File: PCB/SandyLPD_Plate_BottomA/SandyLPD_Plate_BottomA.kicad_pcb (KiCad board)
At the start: 2 copper layers, 127.4 x 83 mm, 163 parts, among them J1 Conn_02x02_Odd_Even, J2 Conn_01x03, J4 Conn_01x10_Pin, J5 USB_C_Receptacle_USB2.0, J6 USB_C_Receptacle_USB2.0, SW1 BOOT_ALT, SW2 RESET_ALT, SW3 SW_DIP_x04, U1 NCP1117-3.3_SOT223, U3 RP2040, U4 W25Q128JVPIQ, Y1 12MHz

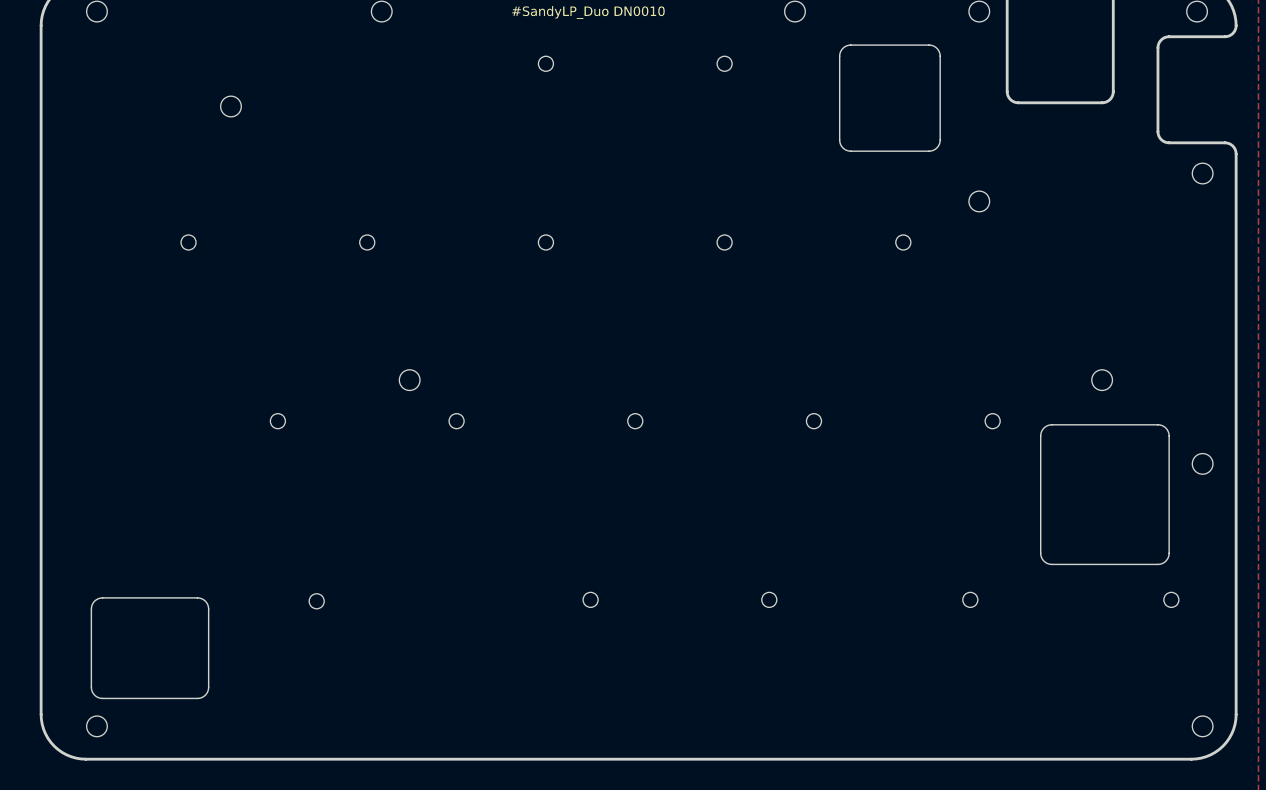
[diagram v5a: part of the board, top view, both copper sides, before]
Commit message: ボトムプレートの穴を大きく
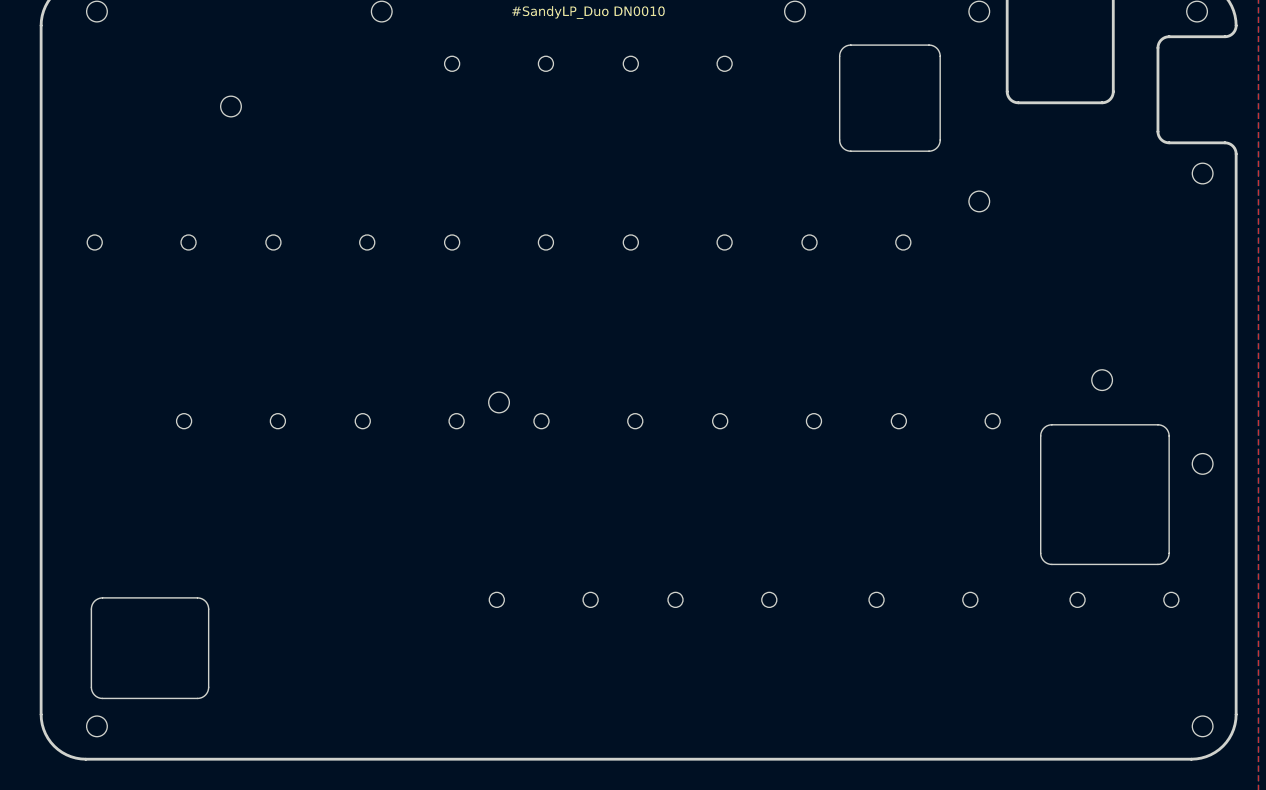
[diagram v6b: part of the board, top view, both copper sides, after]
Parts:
- removed H1, H10, H11, H12, H14, H15, H16, H17, H2, H3, H4, H5, H6, H7, H8, H9: MountingHole, locallib:Kailh_socket_ChocV2_cutout_type2
- removed H13: MountingHole, locallib:Kailh_socket_ChocV2_and_RotaryEncoder_cutout_type2
- moved H_btm_1 9.82 mm to (75.8, 77.0)

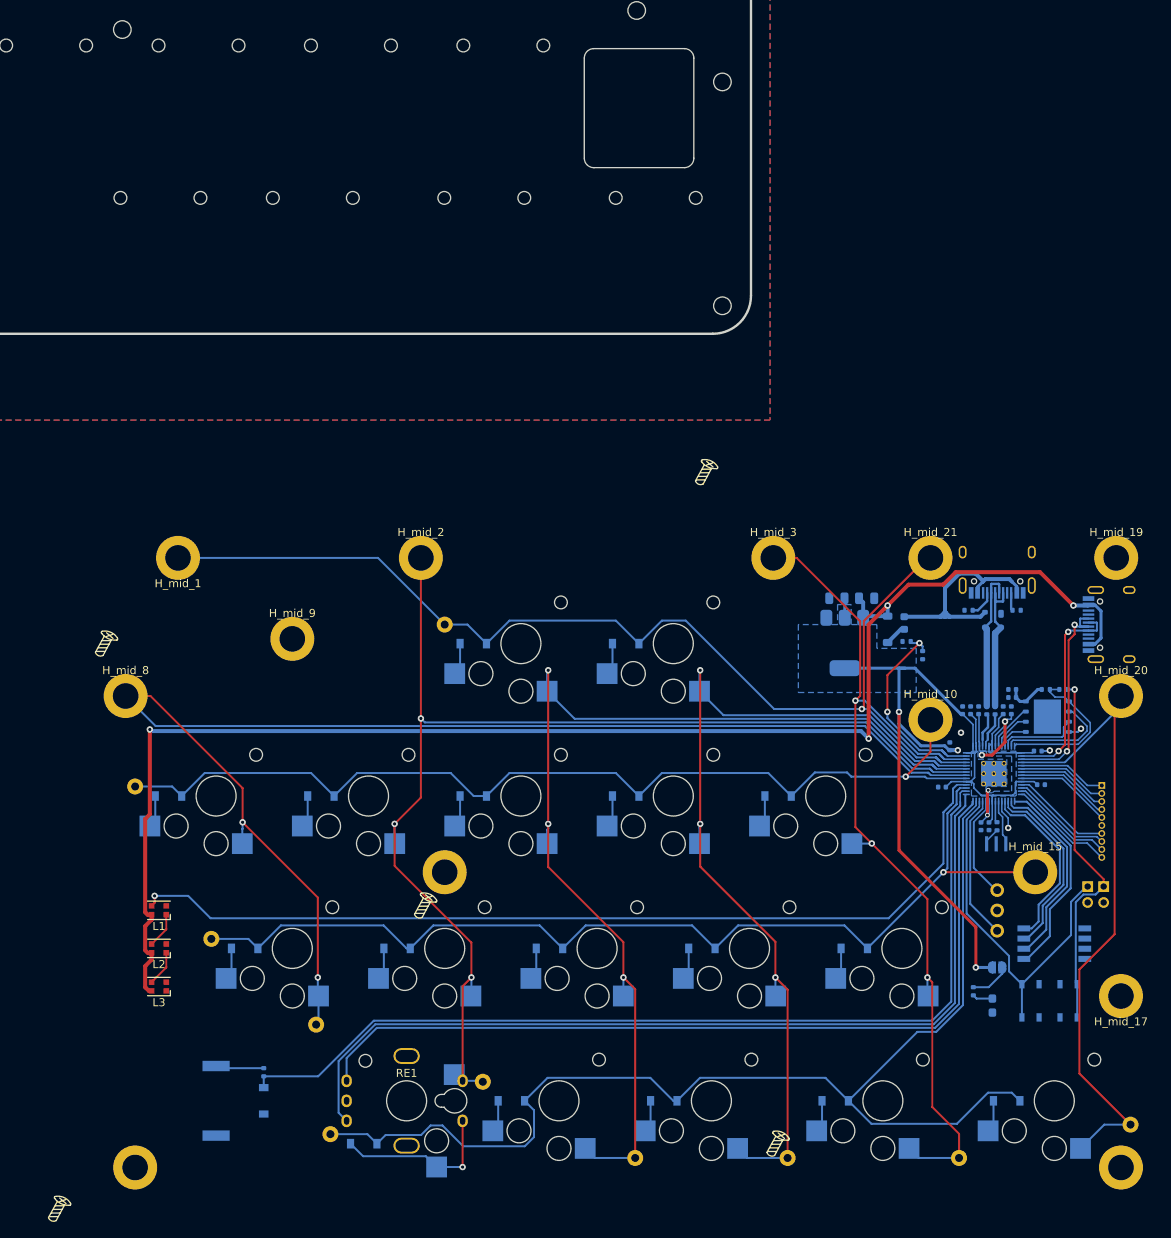
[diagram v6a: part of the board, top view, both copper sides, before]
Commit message: 電源LED位置調整。ボトムA,Bのリセット穴サイズ変更。Fusion用STEP出力。
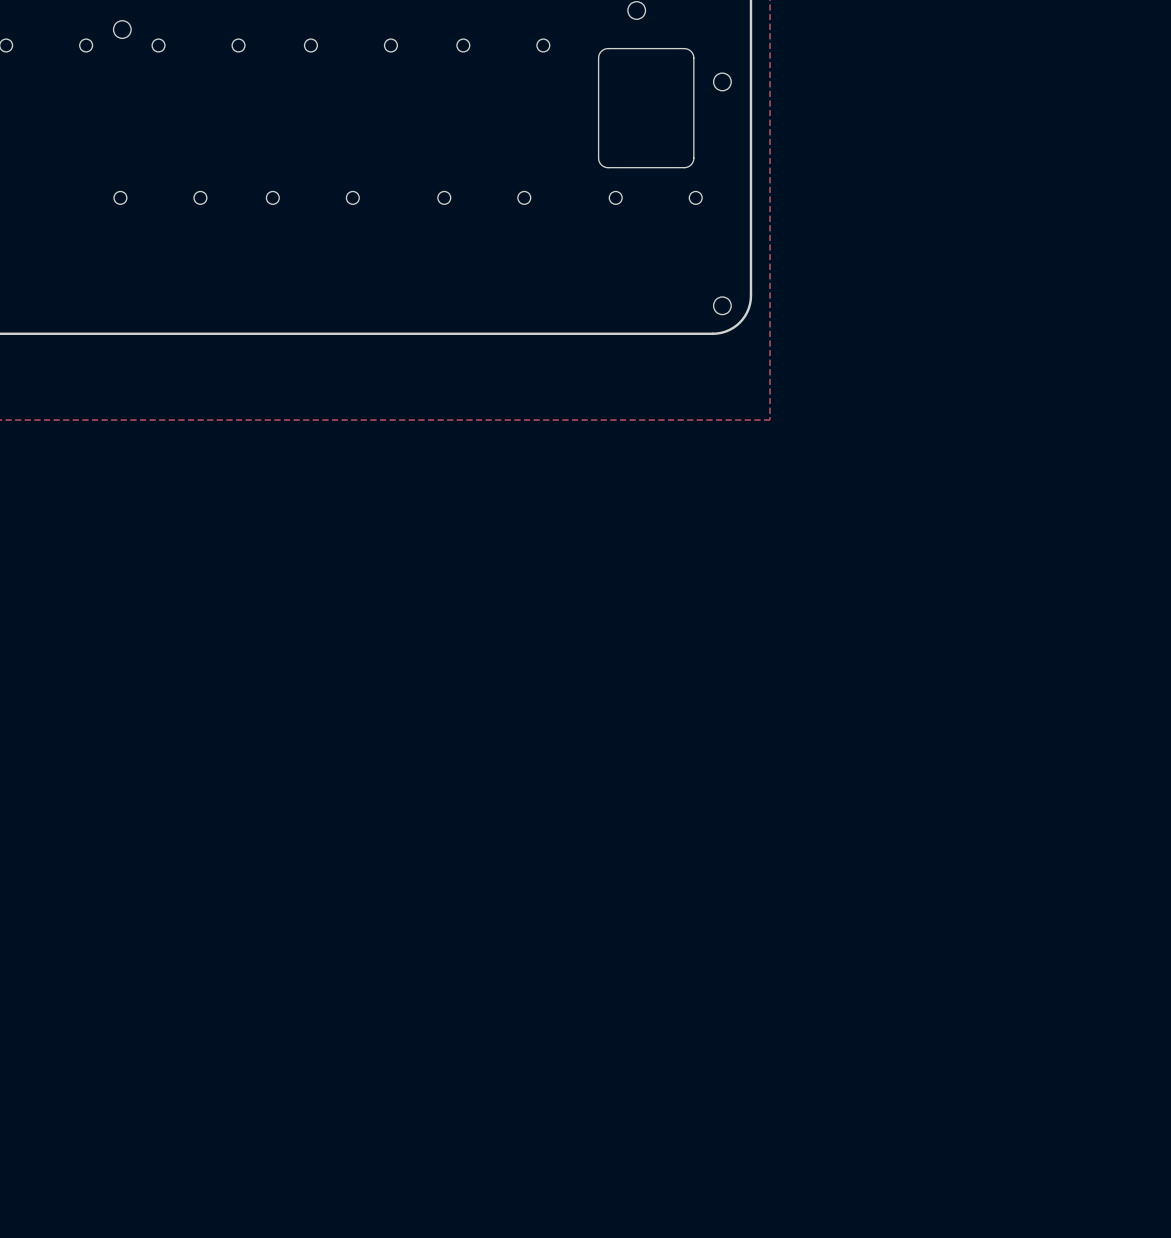
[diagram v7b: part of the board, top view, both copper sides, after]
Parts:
- removed C1, C2: 10u, Capacitor_SMD:C_0805_2012Metric
- removed C10, C11, C12, C3, C4, C5, C6, C7, C8, C9: 100n, Capacitor_SMD:C_0402_1005Metric
- removed C13, C14, C15: 2.2uF, Capacitor_SMD:C_0402_1005Metric
- removed D1, D15, D16, D17, D18, D19, D2, D25, D26, D27, D28, D33, D35, D5, D6, D7, D8, D9: D, locallib:D_SOD-123_Emphasized_Direction_Line_Reference_on_bottom
- removed D36: PRTR5V0U2X, Package_TO_SOT_SMD:SOT-143
- removed F1: Fuse, Fuse:Fuse_0603_1608Metric
- removed the H_btm_1 at (116.1, 182.3)
- removed the H_btm_3 at (77.4, 219.3)
- removed the H_btm_4 at (200.7, 219.3)
- removed the H_mid_1 at (82.8, 143.1)
- removed the H_mid_10 at (176.8, 163.3)
- removed the H_mid_15 at (189.9, 182.3)
- removed the H_mid_17 at (200.7, 197.8)
- removed the H_mid_19 at (200.1, 143.1)
- removed the H_mid_2 at (113.1, 143.1)
- removed the H_mid_20 at (200.7, 160.3)
- removed the H_mid_21 at (176.8, 143.1)
- removed the H_mid_3 at (157.2, 143.1)
- removed H_mid_8: MountingHole, locallib:MountingHole_M2_Through-hole_tap_THC-0.8-x-2
- removed the H_mid_9 at (97.1, 153.2)
- removed J1: Conn_02x02_Odd_Even, locallib:PinHeader_2x02_P2.00mm_Vertical_2pair
- removed J2: Conn_01x03, locallib:PinHeader_1x03_P2.54mm_Vertical_All_circle
- removed J4: Conn_01x10_Pin, Connector_PinHeader_1.00mm:PinHeader_1x10_P1.00mm_Vertical
- removed J5, J6: USB_C_Receptacle_USB2.0, locallib:USB_C_Receptacle_HRO_TYPE-C-31-M-12
- removed JP1: SolderJumper_2_Open, Jumper:SolderJumper-2_P1.3mm_Open_RoundedPad1.0x1.5mm
- removed L1, L2, L3: WS2812B-2020, LED_SMD:LED_WS2812B-2020_PLCC4_2.0x2.0mm
- removed LS1: Speaker, Buzzer_Beeper:Buzzer_Murata_PKMCS0909E
- removed R1, R5, R6, R9: 1k, Resistor_SMD:R_0402_1005Metric
- removed R10, R11: 5.1k, Resistor_SMD:R_0402_1005Metric
- removed R12: 5.6k, Resistor_SMD:R_0402_1005Metric
- removed R2, R3: 27, Resistor_SMD:R_0402_1005Metric
- removed R4, R8: 10k, Resistor_SMD:R_0402_1005Metric
- removed the REF** at (157.7, 218.9)
- removed the REF** at (77.7, 161.9)
- removed the REF** at (160.8, 134.1)
- removed the REF** at (84.3, 137.6)
- removed the REF** at (175.1, 168.5)
- removed the REF** at (110.8, 138.3)
- removed the REF** at (84.0, 135.3)
- removed the REF** at (174.5, 166.9)
- removed the REF** at (66.7, 225.5)
- removed the REF** at (73.8, 156.5)
- removed the REF** at (160.4, 132.3)
- removed the REF** at (67.9, 227.0)
- removed the REF** at (171.4, 133.9)
- removed the REF** at (77.2, 160.3)
- removed the REF** at (164.3, 132.3)
- removed the REF** at (170.9, 132.3)
- removed the REF** at (164.9, 133.8)
- removed the REF** at (94.7, 156.7)
- removed the REF** at (156.6, 219.0)
- removed the REF** at (95.1, 158.3)
- removed the REF** at (73.8, 156.3)
- removed the REF** at (148.8, 134.9)
- removed the REF** at (113.7, 189.1)
- removed the REF** at (110.4, 136.7)
- removed the REF** at (113.1, 189.2)
- removed SD1: Schottky diode, Diode_SMD:D_SOD-123
- removed STLED1: LED_GREEN, LED_SMD:LED_0603_1608Metric_Pad1.05x0.95mm_HandSolder
- removed SW1: BOOT_ALT, Button_Switch_SMD:SW_SPST_PTS810
- removed SW2: RESET_ALT, Button_Switch_SMD:SW_SPST_PTS810
- removed SW3: SW_DIP_x04, Button_Switch_SMD:SW_DIP_SPSTx04_Slide_Copal_CHS-04B_W7.62mm_P1.27mm
- removed SW_1: W, locallib:Kailh_socket_ChocV2
- removed SW_15: Z, locallib:Kailh_socket_ChocV2
- removed SW_16: X, locallib:Kailh_socket_ChocV2
- removed SW_17: C, locallib:Kailh_socket_ChocV2
- removed SW_18: V, locallib:Kailh_socket_ChocV2
- removed SW_19: B, locallib:Kailh_socket_ChocV2
- removed SW_2: E, locallib:Kailh_socket_ChocV2
- removed SW_25: L_RE, locallib:ChocV2_AND_RotaryEncoder_Alps_EC11K-Switch_Vertical_H20mm_NPTH_MP_minimal
- removed SW_27: LALT, locallib:Kailh_socket_ChocV2
- removed SW_28: LSPC, locallib:Kailh_socket_ChocV2
- removed SW_29: L_CNT, locallib:Kailh_socket_ChocV2
- removed SW_5: LCTL, locallib:Kailh_socket_ChocV2
- removed SW_6: A, locallib:Kailh_socket_ChocV2
- removed SW_7: S, locallib:Kailh_socket_ChocV2
- removed SW_8: D, locallib:Kailh_socket_ChocV2
- removed SW_9: F, locallib:Kailh_socket_ChocV2
- removed SW_LWIN1: LWIN, locallib:Kailh_socket_ChocV2
- removed T_L_C0, T_L_C1, T_L_C2, T_L_C3, T_L_C4, T_L_C5, T_L_R0, T_L_R1, T_L_R2, T_L_R3: Conn_01x01, locallib:TestPoint_THTPad_D2.0mm_Drill1.0mm
- removed U1: NCP1117-3.3_SOT223, Package_TO_SOT_SMD:SOT-223-3_TabPin2
- removed U3: RP2040, locallib:RP2040-QFN-56
- removed U4: W25Q128JVPIQ, Package_SON:WSON-8-1EP_6x5mm_P1.27mm_EP3.4x4.3mm
- removed Y1: 12MHz, Crystal:Resonator_SMD_Murata_CSTxExxV-3Pin_3.0x1.1mm
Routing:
- net (no net): track 905.9 -> 0.00 mm, vias 13 -> 0
- net +5V: track 186.2 -> 0.00 mm, vias 4 -> 0
- net L_row3: track 148.8 -> 0.00 mm
- net L_col2: track 137.1 -> 0.00 mm, vias 3 -> 0
- net +3V3: track 127.3 -> 0.00 mm, vias 3 -> 0
- net L_Audio: track 118.6 -> 0.00 mm
- net L_col3: track 118.3 -> 0.00 mm, vias 3 -> 0
- net L_LED: track 115.7 -> 0.00 mm, vias 1 -> 0
- net L_RE_B: track 114.6 -> 0.00 mm
- net L_RE_A: track 108.3 -> 0.00 mm
- net L_RESET: track 46.3 -> 0.00 mm
- net L_USB_BOOT: track 45.8 -> 0.00 mm, vias 1 -> 0
- net VBUS: track 28.8 -> 0.00 mm
- net L_RX: track 27.2 -> 0.00 mm, vias 2 -> 0
- net L_VBUS_detection: track 26.8 -> 0.00 mm, vias 2 -> 0
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- removed copper zone on B.Cu, net (none)
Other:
- board text removed: "Through-hole tap head diameter"
- board text removed: "参考 Base基板 左手"

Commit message: 不要アイコン削除
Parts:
- removed the REF** at (99.0, 27.3)
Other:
- board text removed: "Back Side"
- board text removed: "Fairness, Justice, Rightness"
- board text removed: "Screw for Top plate"
